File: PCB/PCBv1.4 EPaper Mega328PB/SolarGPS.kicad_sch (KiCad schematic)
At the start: 53 parts, among them J1 Conn_01x24_Female, J2 GND, J3 GND, J4 AVR-ISP-6, J5 Solar2+, J6 Solar1+, J7 Screw_Terminal_01x01, J8 Conn_01x04_Male, Q1 Q_NMOS_GSD, U1 TPS63802, U2 MAX-M10Q, U3 ATmega328PB-M, U6 LIS3DH, Y1 32.768

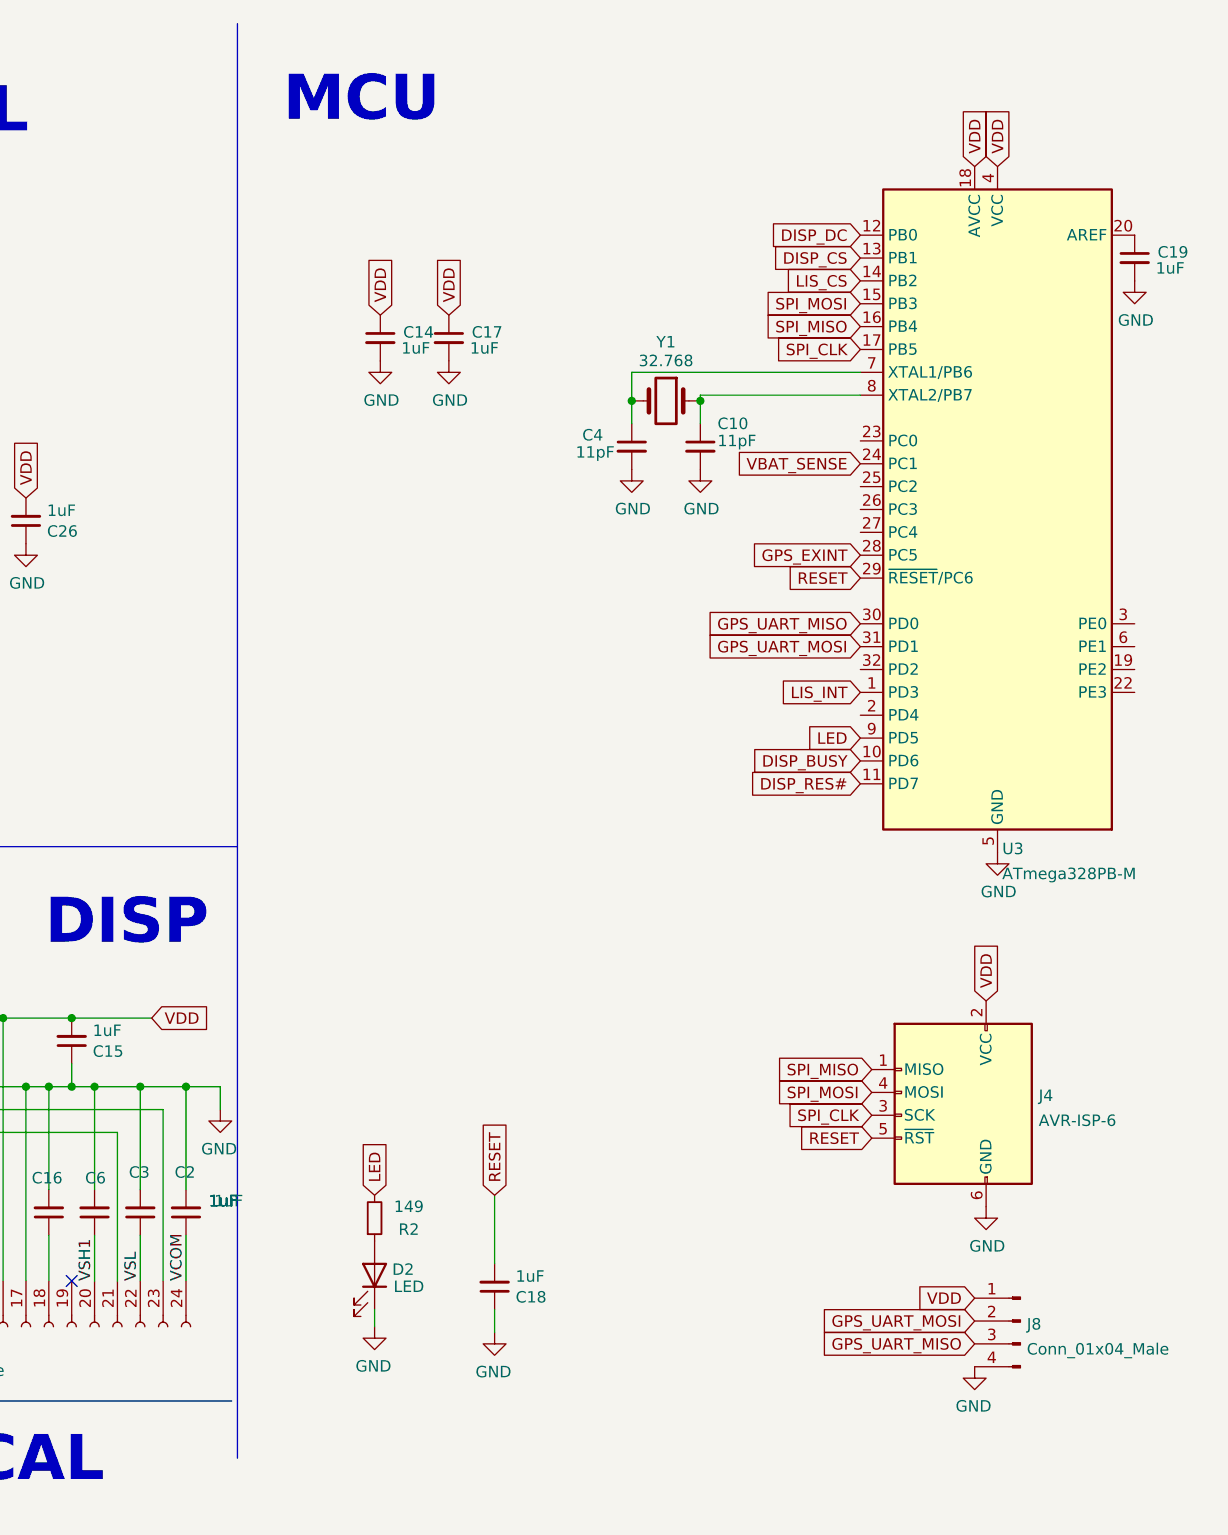
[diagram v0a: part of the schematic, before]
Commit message: add tqfp footprint
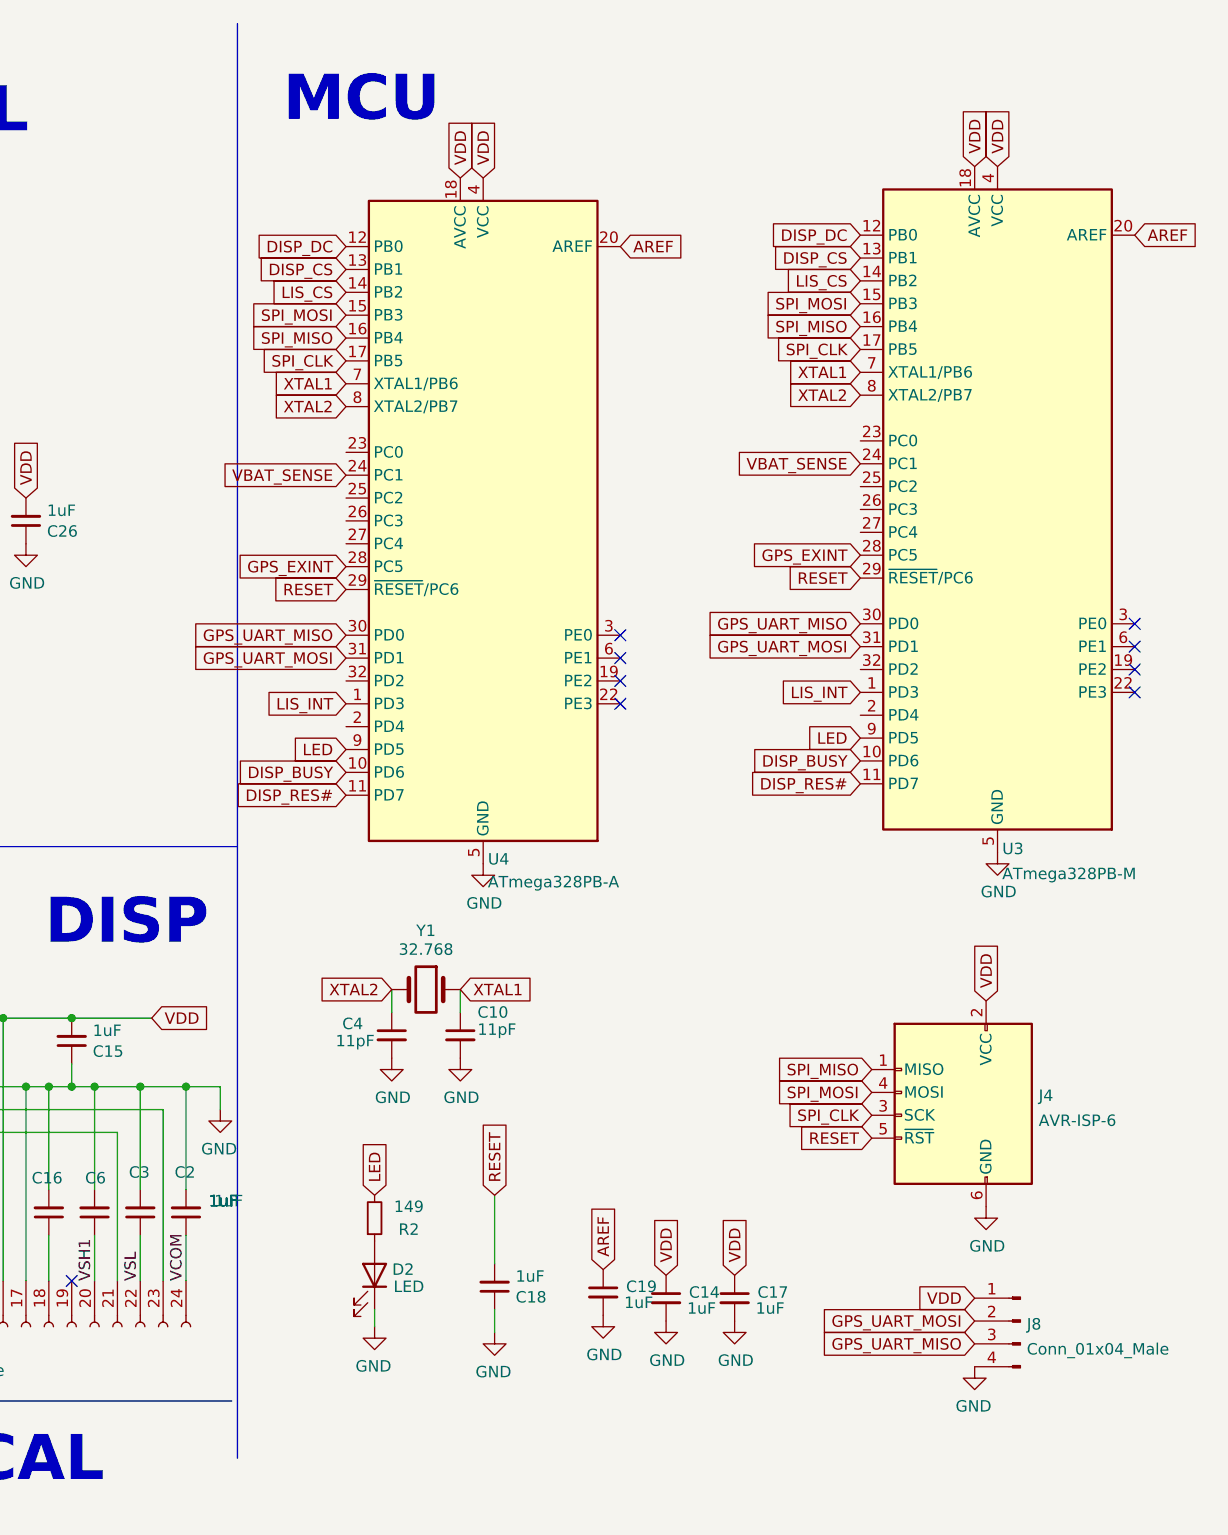
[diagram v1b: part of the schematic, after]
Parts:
- added U4: ATmega328PB-A, Package_QFP:TQFP-32_7x7mm_P0.8mm, symbol MCU_Microchip_ATmega:ATmega328PB-A
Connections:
- net DISP_BUSY: now also U4.10 (PD6)
- net DISP_CS: now also U4.13 (PB1)
- net DISP_DC: now also U4.12 (PB0)
- net DISP_RES#: now also U4.11 (PD7)
- net GND: now also U4.21 (GND), U4.5 (GND)
- net GPS_EXINT: now also U4.28 (PC5)
- net GPS_UART_MISO: now also U4.30 (PD0)
- net GPS_UART_MOSI: now also U4.31 (PD1)
- net LED: now also U4.9 (PD5)
- net LIS_CS: now also U4.14 (PB2)
- net LIS_INT: now also U4.1 (PD3)
- net RESET: now also U4.29 (~{RESET}/PC6)
- net SPI_CLK: now also U4.17 (PB5)
- net SPI_MISO: now also U4.16 (PB4)
- net SPI_MOSI: now also U4.15 (PB3)
- net VBAT_SENSE: now also U4.24 (PC1)
- net VDD: now also U4.18 (AVCC), U4.4 (VCC)
- net XTAL2: now reaches C4.1, Y1.2
- net XTAL2: now also U3.8 (XTAL2/PB7), U4.8 (XTAL2/PB7); no longer U3.7 (XTAL1/PB6)
- net XTAL1: now reaches C10.1, Y1.1
- net XTAL1: now also U3.7 (XTAL1/PB6), U4.7 (XTAL1/PB6); no longer U3.8 (XTAL2/PB7)
- net AREF: now reaches C19.1, U3.20 (AREF)
- net AREF: now also U4.20 (AREF)
- no-connect marks 17 -> 25
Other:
- moved on the sheet: C10, C14, C17, C4, Y1

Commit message: reduce power BOM
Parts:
- removed C11: 10nF, Capacitor_SMD:C_0603_1608Metric, symbol Device:C_Small
- removed C12: 47uF, Capacitor_SMD:C_0805_2012Metric, symbol Device:C_Small
- removed C13, C7: 1uF, Capacitor_SMD:C_0603_1608Metric, symbol Device:C_Small
- removed L2: 0.47uH, Inductor_SMD:L_0806_2016Metric, symbol Device:L_Small
- removed R12, R13: 1M, Resistor_SMD:R_0603_1608Metric, symbol Device:R_Small
- removed R4: 91k, Resistor_SMD:R_0603_1608Metric, symbol Device:R_Small
- removed U1: TPS63802, Margo_Lib:VREG_TPS63802DLAR, symbol SolarGPS-rescue:TPS63802-VeridianDesigns
- added Q2: Q_NMOS_GSD, Package_TO_SOT_SMD:SOT-23, symbol Device:Q_NMOS_GSD
- R1: value 432k -> 1M
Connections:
- net GND: now also Q2.3 (D); no longer C10.2, C14.2, C17.2, C18.1, C19.2, C4.2, C8.2, D2.1 (K), J2.1 (Pin_1), J3.1 (Pin_1), J4.6 (GND), U3.21 (GND), U3.33 (GND), U3.5 (GND), U4.21 (GND), U4.5 (GND)
- net VBAT: now also C14.1, C15.2, C17.1, C26.2, C5.1, J1.15 (Pin_15), J1.16 (Pin_16), J4.2 (VCC), J8.1 (Pin_1), L1.1, U2.6 (V_BCKP), U2.7 (VCC_IO), U2.8 (VCC), U3.18 (AVCC), U3.4 (VCC), U4.18 (AVCC), U4.4 (VCC), U6.1 (VDD_IO), U6.14 (VDD)
- net GNDPWR: now reaches R1.1
- net GNDPWR: now also C10.2, C14.2, C17.2, C18.1, C19.2, C4.2, C8.2, D2.1 (K), J2.1 (Pin_1), J3.1 (Pin_1), J4.6 (GND), U3.21 (GND), U3.33 (GND), U3.5 (GND), U4.21 (GND), U4.5 (GND), Q2.2 (S)
- net ACCSW: now reaches U4.23 (PC0)
- net ACCSW: now also R1.2, U3.23 (PC0), Q2.1 (G)
- removed net VDD: C14.1, C15.2, C17.1, C26.2, C5.1, J1.15 (Pin_15), J1.16 (Pin_16), J4.2 (VCC), J8.1 (Pin_1), L1.1, R1.2, U2.6 (V_BCKP), U2.7 (VCC_IO), U2.8 (VCC), U3.18 (AVCC), U3.4 (VCC), U4.18 (AVCC), U4.4 (VCC), U6.1 (VDD_IO), U6.14 (VDD)
- no-connect marks 25 -> 24
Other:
- note removed: "ANALOG"
- note removed: "VOUT = 2.87"
- moved on the sheet: C10, C14, C17, C18, C19, C4, D2, J2, J3, J8, R2, U3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
